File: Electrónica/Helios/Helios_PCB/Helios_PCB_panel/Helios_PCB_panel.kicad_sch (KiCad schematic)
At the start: 46 parts, among them M0_0 Conn_01x04_Pin, M0_1 Conn_01x04_Pin, M0_2 Conn_01x04_Pin, M0_3 Conn_01x04_Pin, M1_0 Conn_01x04_Pin, M1_1 Conn_01x04_Pin, M1_2 Conn_01x04_Pin, M1_3 Conn_01x04_Pin, M2_0 Conn_01x04_Pin, M2_1 Conn_01x04_Pin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

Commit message: PCBs ready for manufacturing
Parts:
- I2C1: value 12VDC -> I2C1
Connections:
- net SCL: now also I2C1.1 (Pin_1); no longer I2C1.2 (Pin_2)
- net SDA: now also I2C1.2 (Pin_2); no longer I2C1.1 (Pin_1)
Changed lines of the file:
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@@
-    )
-  )
-  (global_label "SCL" (shape output) (at 236.22 30.48 0) (fields_autoplaced)
-    (effects (font (size 1.27 1.27)) (justify left))
-    (property "Intersheetrefs" "${INTERSHEET_REFS}" (at 242.6334 30.48 0)
-      (effects (font (size 1.27 1.27)) (justify left) hide)
     )
   )
@@
     )
   )
+  (global_label "SCL" (shape output) (at 236.22 27.94 0) (fields_autoplaced)
+    (effects (font (size 1.27 1.27)) (justify left))
+    (property "Intersheetrefs" "${INTERSHEET_REFS}" (at 242.6334 27.94 0)
+      (effects (font (size 1.27 1.27)) (justify left) hide)
+    )
+  )
   (global_label "EN1" (shape input) (at 24.13 85.09 180) (fields_autoplaced)
     (effects (font (size 1.27 1.27)) (justify right))
@@
     )
   )
+  (global_label "SDA" (shape output) (at 236.22 30.48 0) (fields_autoplaced)
+    (effects (font (size 1.27 1.27)) (justify left))
+    (property "Intersheetrefs" "${INTERSHEET_REFS}" (at 242.6939 30.48 0)
+      (effects (font (size 1.27 1.27)) (justify left) hide)
+    )
+  )
   (global_label "EN2" (shape input) (at 209.55 85.09 180) (fields_autoplaced)
     (effects (font (size 1.27 1.27)) (justify right))
@@
     (property "Intersheetrefs" "${INTERSHEET_REFS}" (at 204.2252 92.71 0)
       (effects (font (size 1.27 1.27)) (justify right) hide)
-    )
-  )
-  (global_label "SDA" (shape output) (at 236.22 27.94 0) (fields_autoplaced)
-    (effects (font (size 1.27 1.27)) (justify left))
-    (property "Intersheetrefs" "${INTERSHEET_REFS}" (at 242.6939 27.94 0)
-      (effects (font (size 1.27 1.27)) (justify left) hide)
     )
   )
@@
     (pin "19")
     (pin "2")
+    (pin "20")
+    (pin "21")
+    (pin "22")
+    (pin "23")
+    (pin "24")
+    (pin "25")
+    (pin "26")
+    (pin "27")
+    (pin "28")
+    (pin "29")
+    (pin "3")
+    (pin "30")
+    (pin "31")
+    (pin "32")
+    (pin "33")
+    (pin "34")
+    (pin "35")
+    (pin "36")
+    (pin "37")
     (pin "38")
-    (pin "37")
-    (pin "36")
-    (pin "35")
-    (pin "34")
-    (pin "33")
-    (pin "32")
-    (pin "31")
-    (pin "30")
-    (pin "29")
-    (pin "3")
-    (pin "28")
-    (pin "27")
-    (pin "26")
-    (pin "25")
-    (pin "24")
-    (pin "23")
-    (pin "22")
-    (pin "21")
-    (pin "20")
     (pin "4")
     (pin "5")
@@
       (effects (font (size 1.27 1.27)))
     )
-    (property "Value" "12VDC" (at 234.95 24.13 0)
-      (effects (font (size 1.27 1.27)))
-    )
+    (property "Value" "I2C1" (at 234.95 24.13 0)
+      (effects (font (size 1.27 1.27)))
+    )

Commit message: Minor Updates
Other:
- note added: "1.0"
- note added: "22/11/2023"
- note added: "Helios Robot - Main Panel"
- note added: "This schematic describes the connections of the Helios Robot's main panel. It is formed by twelve motor drivers controlled by a ESP32 module. The board includes a power and I2C interface to feed the robot's modules. It also has an extra SPI interface and GPIO pins for future expansions or extra functionalities."
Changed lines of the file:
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@@
     (stroke (width 0) (type default))
+  )
+  (text "22/11/2023" (at 206.248 193.802 0)
+    (effects (font (size 1.27 1.27)) (justify left bottom))
+  )
+  (text "1.0" (at 268.478 193.802 0)
+    (effects (font (size 1.27 1.27)) (justify left bottom))
+  )
+  (text "This schematic describes the connections of the Helios Robot's main panel. It is formed by twelve motor\ndrivers controlled by a ESP32 module. The board includes a power and I2C interface to feed the robot's\nmodules. It also has an extra SPI interface and GPIO pins for future expansions or extra functionalities."
+    (at 179.578 173.99 0)
+    (effects (font (size 1.27 1.27)) (justify left bottom))
+  )
+  (text "Helios Robot - Main Panel" (at 186.944 190.246 0)
+    (effects (font (size 1.27 1.27)) (justify left bottom))
   )
   (global_label "MOSI" (shape output) (at 267.97 41.91 0) (fields_autoplaced)

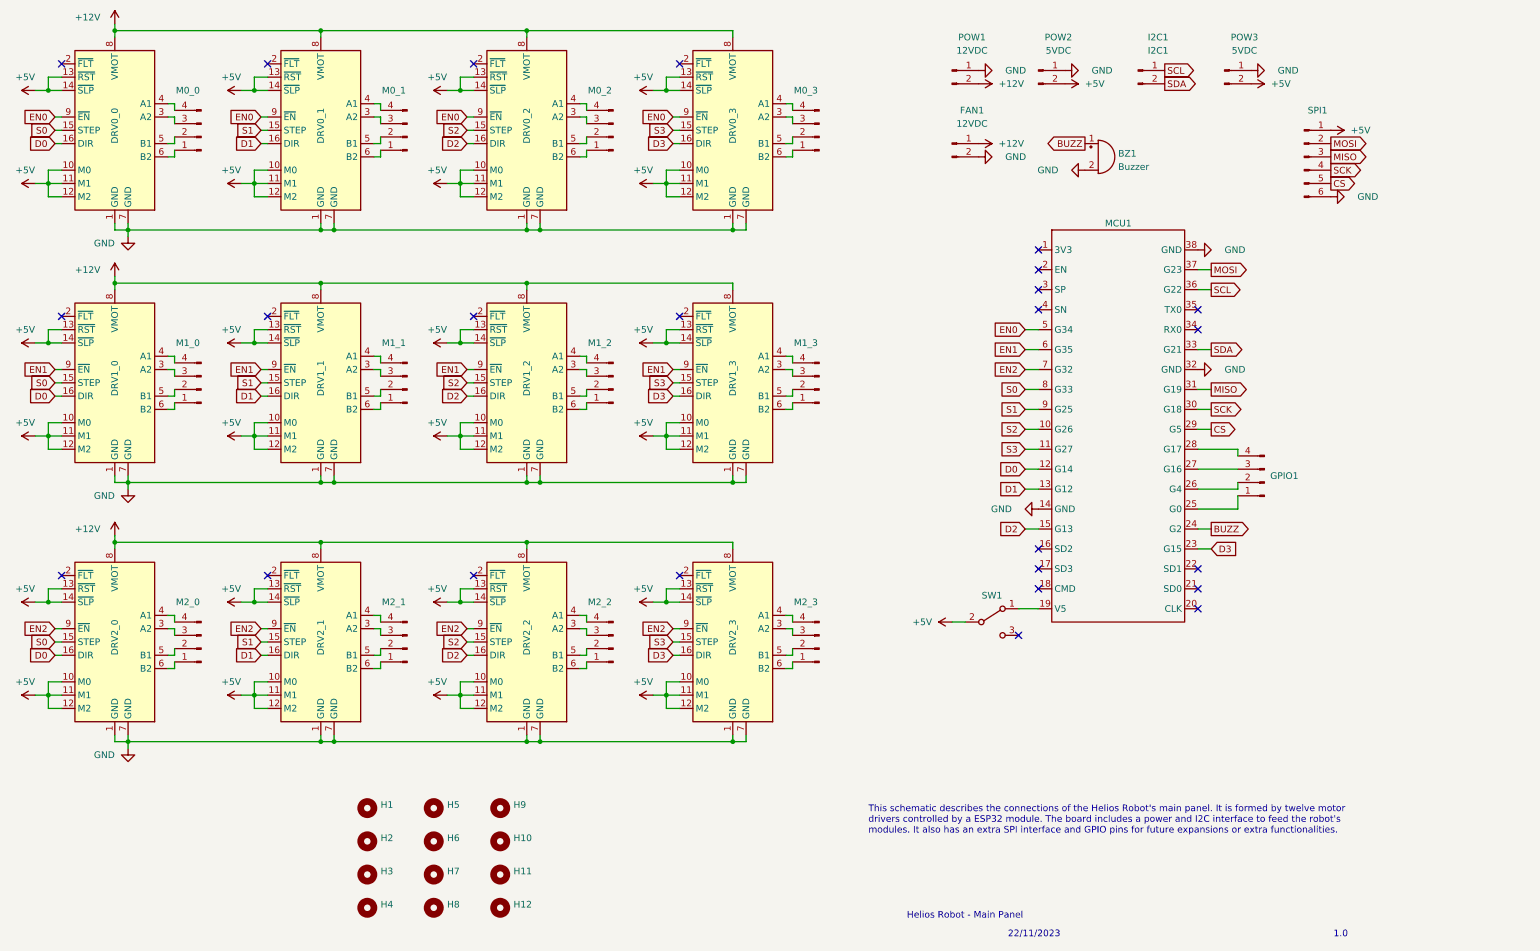
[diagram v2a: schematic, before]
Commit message: Generated STL files for pulley actuator
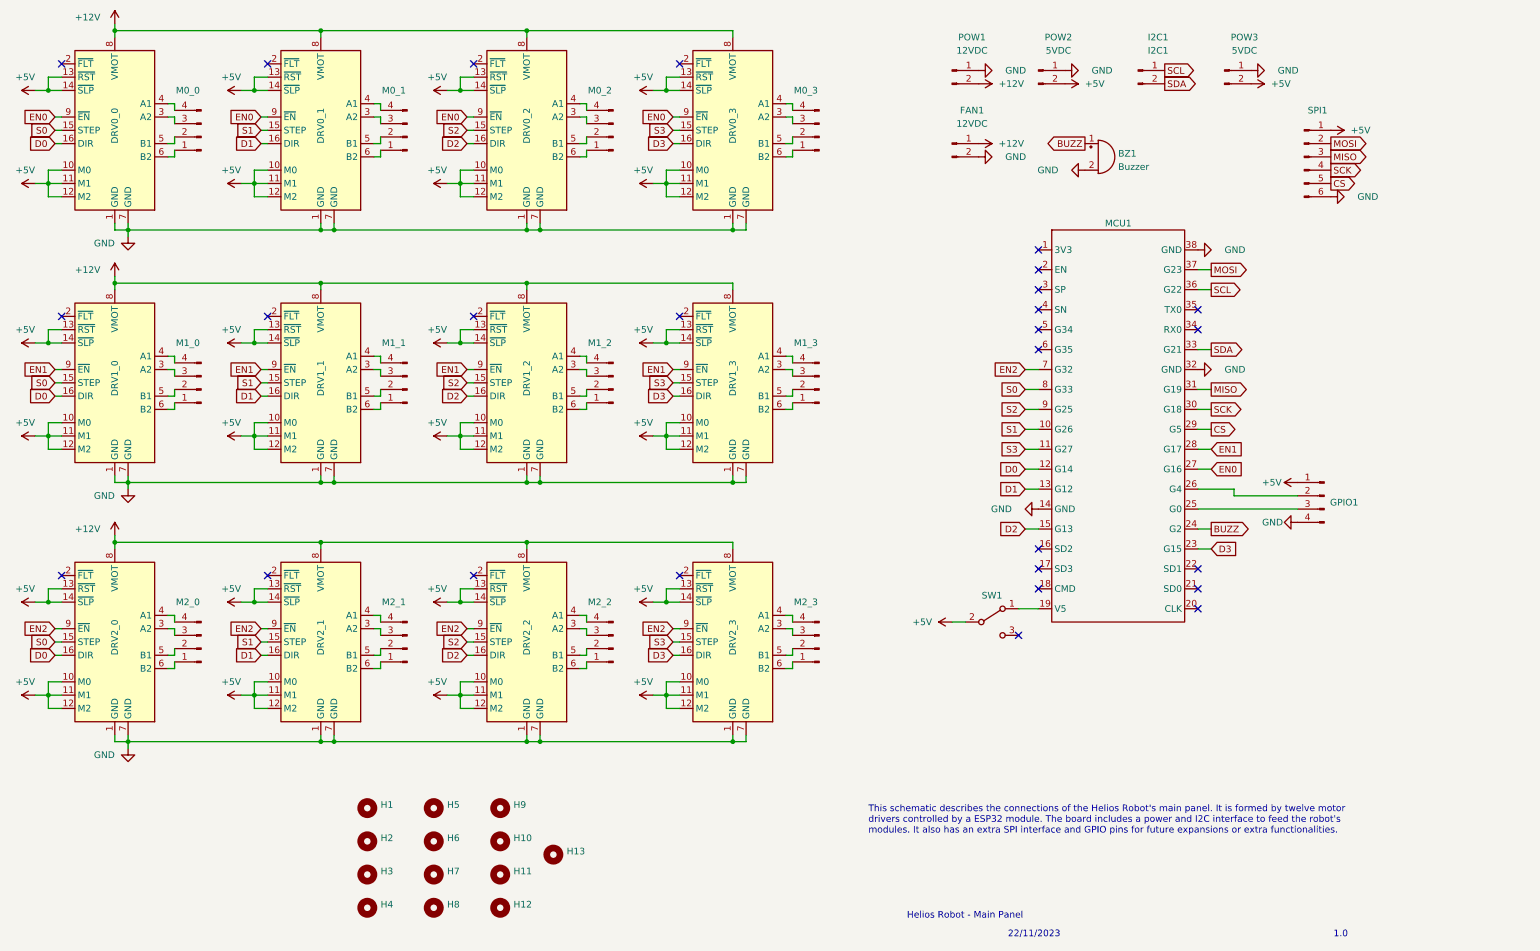
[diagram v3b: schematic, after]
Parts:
- added H13: MountingHole, MountingHole:MountingHole_8.4mm_M8, symbol Mechanical:MountingHole
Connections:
- net +5V: now also GPIO1.1 (Pin_1)
- net EN0: now also MCU1.27 (G16); no longer MCU1.5 (G34)
- net EN1: now also MCU1.28 (G17); no longer MCU1.6 (G35)
- net GND: now also GPIO1.4 (Pin_4)
- net S1: now also MCU1.10 (G26); no longer MCU1.9 (G25)
- net S2: now also MCU1.9 (G25); no longer MCU1.10 (G26)
- net at MCU1.25 (G0): now also GPIO1.3 (Pin_3); no longer GPIO1.1 (Pin_1)
- no-connect marks 25 -> 27
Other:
- moved on the sheet: GPIO1
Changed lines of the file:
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@@
   (no_connect (at 104.14 74.93))
   (no_connect (at 212.09 69.85))
+  (no_connect (at 212.09 81.28))
   (no_connect (at 212.09 73.66))
   (no_connect (at 64.77 124.46))
@@
   (no_connect (at 25.4 26.67))
   (no_connect (at 212.09 66.04))
+  (no_connect (at 212.09 77.47))
   (wire (pts (xy 86.36 134.62) (xy 85.09 134.62))
     (stroke (width 0) (type default))
@@
     (stroke (width 0) (type default))
   )
-  (wire (pts (xy 209.55 81.28) (xy 212.09 81.28))
-    (stroke (width 0) (type default))
-  )
   (wire (pts (xy 124.46 142.24) (xy 125.73 142.24))
     (stroke (width 0) (type default))
@@
     (stroke (width 0) (type default))
   )
-  (wire (pts (xy 250.19 100.33) (xy 242.57 100.33))
-    (stroke (width 0) (type default))
-  )
   (wire (pts (xy 124.46 132.08) (xy 125.73 132.08))
     (stroke (width 0) (type default))
@@
     (stroke (width 0) (type default))
   )
-  (wire (pts (xy 250.19 101.6) (xy 250.19 100.33))
-    (stroke (width 0) (type default))
-  )
   (wire (pts (xy 99.06 97.79) (xy 101.6 97.79))
     (stroke (width 0) (type default))
@@
     (stroke (width 0) (type default))
   )
+  (wire (pts (xy 242.57 107.95) (xy 249.4765 107.95))
+    (stroke (width 0) (type default))
+  )
   (wire (pts (xy 101.6 46.99) (xy 104.14 46.99))
     (stroke (width 0) (type default))
@@
     (stroke (width 0) (type default))
   )
+  (wire (pts (xy 249.4765 109.22) (xy 261.62 109.22))
+    (stroke (width 0) (type default))
+  )
   (wire (pts (xy 114.3 58.42) (xy 114.3 57.15))
     (stroke (width 0) (type default))
@@
     (stroke (width 0) (type default))
   )
+  (wire (pts (xy 245.11 100.33) (xy 242.57 100.33))
+    (stroke (width 0) (type default))
+  )
   (wire (pts (xy 101.6 49.53) (xy 101.6 52.07))
     (stroke (width 0) (type default))
@@
     (stroke (width 0) (type default))
   )
+  (wire (pts (xy 245.11 104.14) (xy 242.57 104.14))
+    (stroke (width 0) (type default))
+  )
   (wire (pts (xy 24.13 41.91) (xy 25.4 41.91))
     (stroke (width 0) (type default))
@@
     (stroke (width 0) (type default))
   )
-  (wire (pts (xy 250.19 107.95) (xy 242.57 107.95))
-    (stroke (width 0) (type default))
-  )
-  (wire (pts (xy 250.19 109.22) (xy 250.19 111.76))
-    (stroke (width 0) (type default))
-  )
   (wire (pts (xy 62.23 49.53) (xy 62.23 52.07))
     (stroke (width 0) (type default))
   )
-  (wire (pts (xy 242.57 104.14) (xy 250.19 104.14))
-    (stroke (width 0) (type default))
-  )
   (wire (pts (xy 86.36 139.7) (xy 85.09 139.7))
     (stroke (width 0) (type default))
@@
     (stroke (width 0) (type default))
   )
-  (wire (pts (xy 250.19 107.95) (xy 250.19 106.68))
-    (stroke (width 0) (type default))
-  )
   (wire (pts (xy 102.87 41.91) (xy 104.14 41.91))
     (stroke (width 0) (type default))
@@
     (stroke (width 0) (type default))
   )
-  (wire (pts (xy 250.19 111.76) (xy 242.57 111.76))
-    (stroke (width 0) (type default))
-  )
   (wire (pts (xy 101.6 80.01) (xy 104.14 80.01))
     (stroke (width 0) (type default))
@@
     (stroke (width 0) (type default))
   )
-  (wire (pts (xy 209.55 77.47) (xy 212.09 77.47))
-    (stroke (width 0) (type default))
-  )
   (wire (pts (xy 125.73 88.9) (xy 125.73 90.17))
     (stroke (width 0) (type default))
@@
     (stroke (width 0) (type default))
   )
+  (wire (pts (xy 249.4765 107.95) (xy 249.4765 109.22))
+    (stroke (width 0) (type default))
+  )
   (wire (pts (xy 59.69 97.79) (xy 62.23 97.79))
     (stroke (width 0) (type default))
@@
     (stroke (width 0) (type default))
   )
+  (wire (pts (xy 242.57 111.76) (xy 261.62 111.76))
+    (stroke (width 0) (type default))
+  )
   (wire (pts (xy 163.83 92.71) (xy 165.1 92.71))
     (stroke (width 0) (type default))
@@
     )
   )
-  (global_label "S2" (shape input) (at 209.55 96.52 180) (fields_autoplaced)
+  (global_label "S1" (shape input) (at 209.55 96.52 180) (fields_autoplaced)
     (effects (font (size 1.27 1.27)) (justify right))
     (property "Intersheetrefs" "${INTERSHEET_REFS}" (at 204.2252 96.52 0)
@@
     )
   )
-  (global_label "EN0" (shape input) (at 209.55 77.47 180) (fields_autoplaced)
-    (effects (font (size 1.27 1.27)) (justify right))
-    (property "Intersheetrefs" "${INTERSHEET_REFS}" (at 202.9552 77.47 0)
-      (effects (font (size 1.27 1.27)) (justify right) hide)
+  (global_label "EN0" (shape input) (at 245.11 104.14 0) (fields_autoplaced)
+    (effects (font (size 1.27 1.27)) (justify left))
+    (property "Intersheetrefs" "${INTERSHEET_REFS}" (at 251.7048 104.14 0)
+      (effects (font (size 1.27 1.27)) (justify left) hide)
     )
   )
@@
     )
   )
-  (global_label "S1" (shape input) (at 209.55 92.71 180) (fields_autoplaced)
+  (global_label "S2" (shape input) (at 209.55 92.71 180) (fields_autoplaced)
     (effects (font (size 1.27 1.27)) (justify right))
     (property "Intersheetrefs" "${INTERSHEET_REFS}" (at 204.2252 92.71 0)
@@
     )
   )
-  (global_label "EN1" (shape input) (at 209.55 81.28 180) (fields_autoplaced)
-    (effects (font (size 1.27 1.27)) (justify right))
-    (property "Intersheetrefs" "${INTERSHEET_REFS}" (at 202.9552 81.28 0)
-      (effects (font (size 1.27 1.27)) (justify right) hide)
+  (global_label "EN1" (shape input) (at 245.11 100.33 0) (fields_autoplaced)
+    (effects (font (size 1.27 1.27)) (justify left))
+    (property "Intersheetrefs" "${INTERSHEET_REFS}" (at 251.7048 100.33 0)
+      (effects (font (size 1.27 1.27)) (justify left) hide)
     )
   )
@@
     )
   )
+  (symbol (lib_id "Mechanical:MountingHole") (at 119.38 177.8 0) (unit 1)
+    (in_bom yes) (on_board yes) (dnp no) (fields_autoplaced)
+    (property "Reference" "H13" (at 121.92 177.165 0)
+      (effects (font (size 1.27 1.27)) (justify left))
+    )
+    (property "Value" "MountingHole" (at 121.92 179.705 0)
+      (effects (font (size 1.27 1.27)) (justify left) hide)
+    )
+    (property "Footprint" "MountingHole:MountingHole_8.4mm_M8" (at 119.38 177.8 0)
+      (effects (font (size 1.27 1.27)) hide)
+    )
+    (property "Datasheet" "~" (at 119.38 177.8 0)
+      (effects (font (size 1.27 1.27)) hide)
+    )
+    (instances
+      (project "Helios_PCB_panel"
+        (path "/5ec27aa6-3ae2-4c2f-8df3-2da048d38998"
+          (reference "H13") (unit 1)
+        )
+      )
+    )
+  )
   (symbol (lib_id "power:+5V") (at 138.43 31.75 90) (unit 1)
     (in_bom yes) (on_board yes) (dnp no)
@@
     )
   )
+  (symbol (lib_id "power:GND") (at 261.62 114.3 270) (unit 1)
+    (in_bom yes) (on_board yes) (dnp no)
+    (property "Reference" "#PWR046" (at 255.27 114.3 0)
+      (effects (font (size 1.27 1.27)) hide)
+    )
+    (property "Value" "GND" (at 258.826 114.3 90)
+      (effects (font (size 1.27 1.27)) (justify right))
+    )
+    (property "Footprint" "" (at 261.62 114.3 0)
+      (effects (font (size 1.27 1.27)) hide)
+    )
+    (property "Datasheet" "" (at 261.62 114.3 0)
+      (effects (font (size 1.27 1.27)) hide)
+    )
+    (pin "1")
+    (instances
+      (project "Helios_PCB_panel"
+        (path "/5ec27aa6-3ae2-4c2f-8df3-2da048d38998"
+          (reference "#PWR046") (unit 1)
+        )
+      )
+    )
+  )
   (symbol (lib_id "Mechanical:MountingHole") (at 109.22 175.26 0) (unit 1)
     (in_bom yes) (on_board yes) (dnp no) (fields_autoplaced)
@@
     )
   )
+  (symbol (lib_id "power:+5V") (at 261.62 106.68 90) (unit 1)
+    (in_bom yes) (on_board yes) (dnp no)
+    (property "Reference" "#PWR047" (at 265.43 106.68 0)
+      (effects (font (size 1.27 1.27)) hide)
+    )
+    (property "Value" "+5V" (at 258.572 106.68 90)
+      (effects (font (size 1.27 1.27)) (justify left))
+    )
+    (property "Footprint" "" (at 261.62 106.68 0)
+      (effects (font (size 1.27 1.27)) hide)
+    )
+    (property "Datasheet" "" (at 261.62 106.68 0)
+      (effects (font (size 1.27 1.27)) hide)
+    )
+    (pin "1")
+    (instances
+      (project "Helios_PCB_panel"
+        (path "/5ec27aa6-3ae2-4c2f-8df3-2da048d38998"
+          (reference "#PWR047") (unit 1)
+        )
+      )
+    )
+  )
   (symbol (lib_id "Connector:Conn_01x02_Pin") (at 212.09 27.94 0) (unit 1)
     (in_bom yes) (on_board yes) (dnp no)
@@
     )
   )
-  (symbol (lib_id "Connector:Conn_01x04_Pin") (at 255.27 106.68 180) (unit 1)
+  (symbol (lib_id "Connector:Conn_01x04_Pin") (at 266.7 109.22 0) (mirror y) (unit 1)
     (in_bom yes) (on_board yes) (dnp no)
-    (property "Reference" "GPIO1" (at 259.08 105.41 0)
+    (property "Reference" "GPIO1" (at 270.51 110.49 0)
       (effects (font (size 1.27 1.27)))
     )
-    (property "Value" "Conn_01x04_Pin" (at 254.635 110.49 0)
+    (property "Value" "Conn_01x04_Pin" (at 266.065 105.41 0)
       (effects (font (size 1.27 1.27)) hide)
     )
-    (property "Footprint" "Connector_PinSocket_2.54mm:PinSocket_1x04_P2.54mm_Vertical" (at 255.27 106.68 0)
+    (property "Footprint" "Connector_PinSocket_2.54mm:PinSocket_1x04_P2.54mm_Vertical" (at 266.7 109.22 0)
       (effects (font (size 1.27 1.27)) hide)
     )
-    (property "Datasheet" "~" (at 255.27 106.68 0)
+    (property "Datasheet" "~" (at 266.7 109.22 0)
       (effects (font (size 1.27 1.27)) hide)
     )
